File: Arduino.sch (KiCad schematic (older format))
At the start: 0 parts

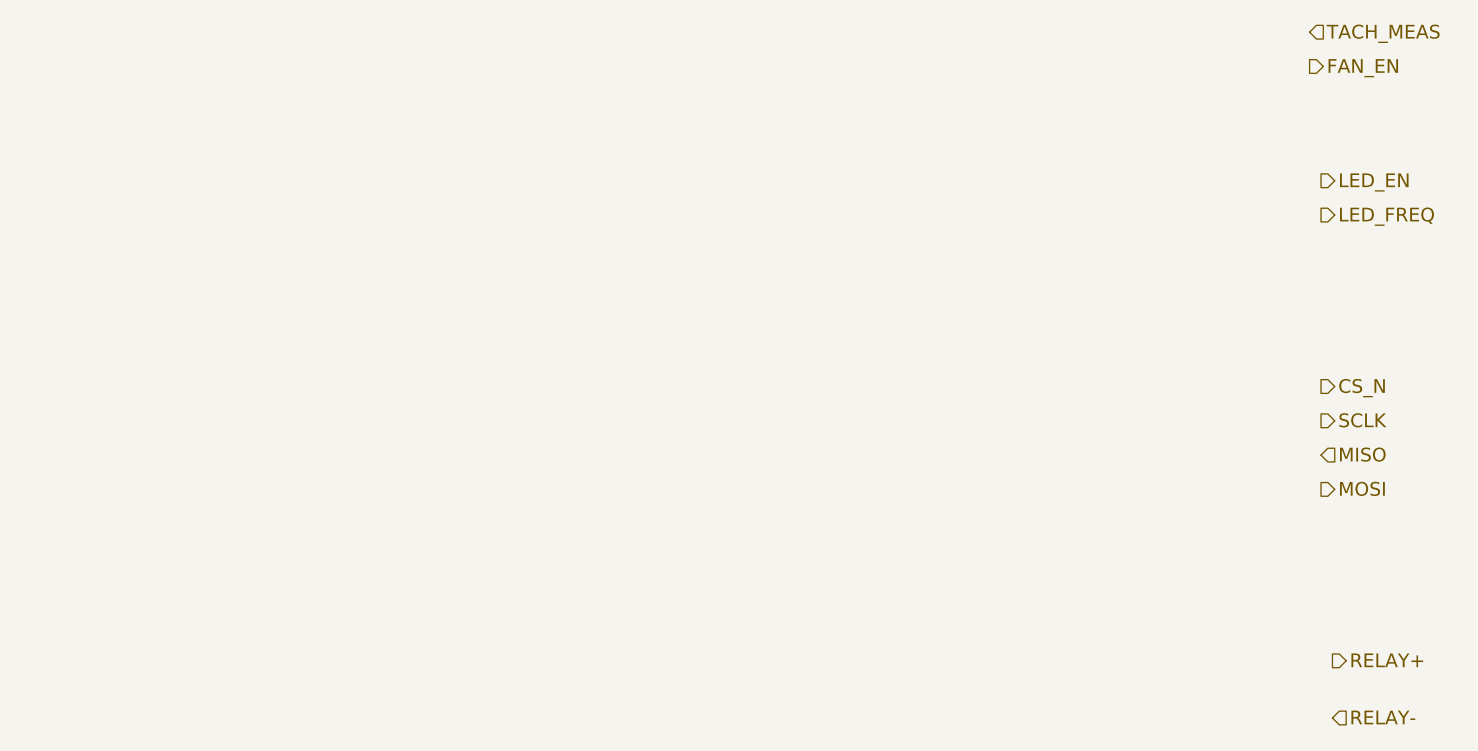
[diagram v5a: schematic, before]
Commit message: Created the Arduino module and then connected all the modules in the main schematic
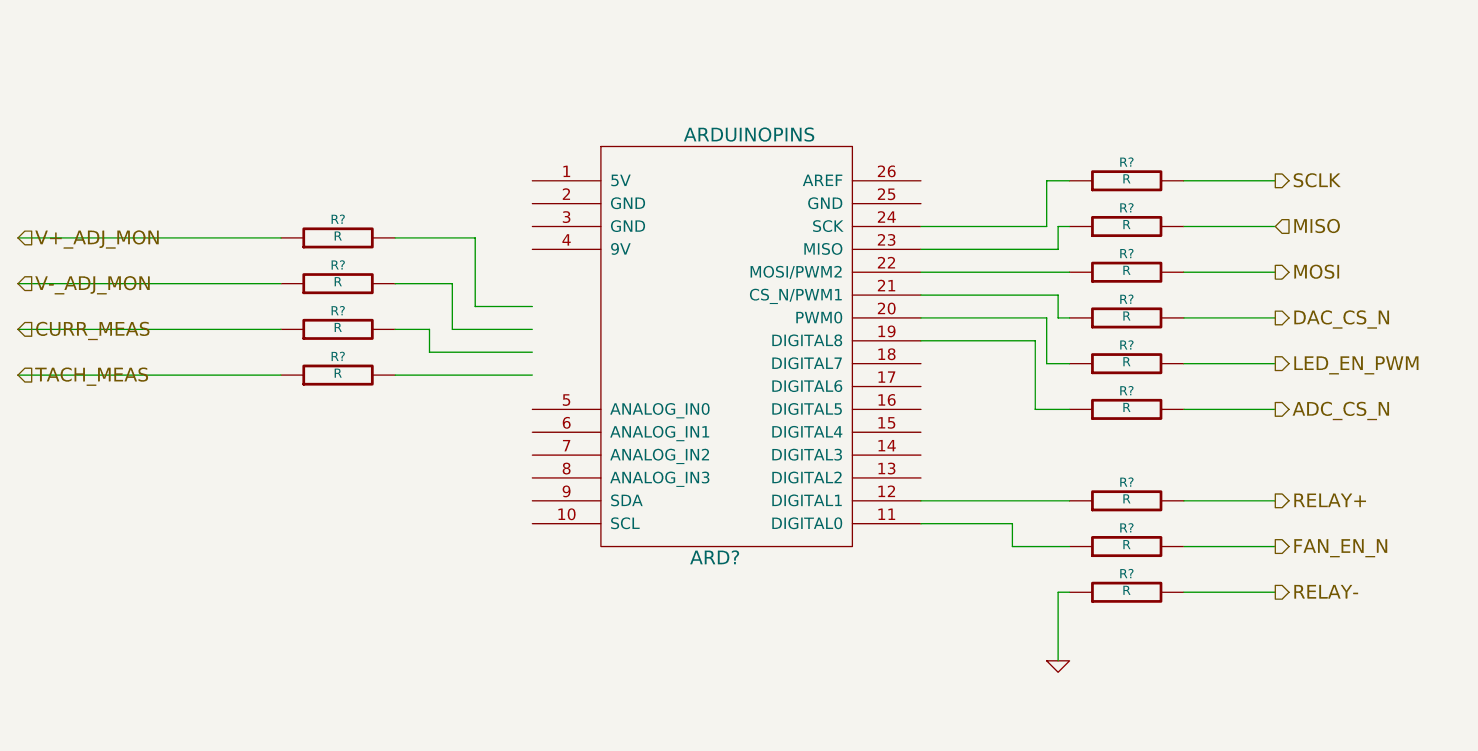
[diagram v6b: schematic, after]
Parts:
- added ARD?: ARDUINOPINS, symbol ARDUINOPINS
- added R? (x13): R, ~, symbol R
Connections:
- net labels added: ADC_CS_N, CURR_MEAS, DAC_CS_N, FAN_EN_N, GND, LED_EN_PWM, V+_ADJ_MON, V-_ADJ_MON
- net labels removed: CS_N, FAN_EN, LED_EN, LED_FREQ
- wire segments 0 -> 45

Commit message: Modified the FAN module and corresponding pins in Arduino module
1) Added FAN_MODE
2) Changed FAN_EN_N to FAN_PWM
3) Used one of the digital PWM pins for FAN_PWM
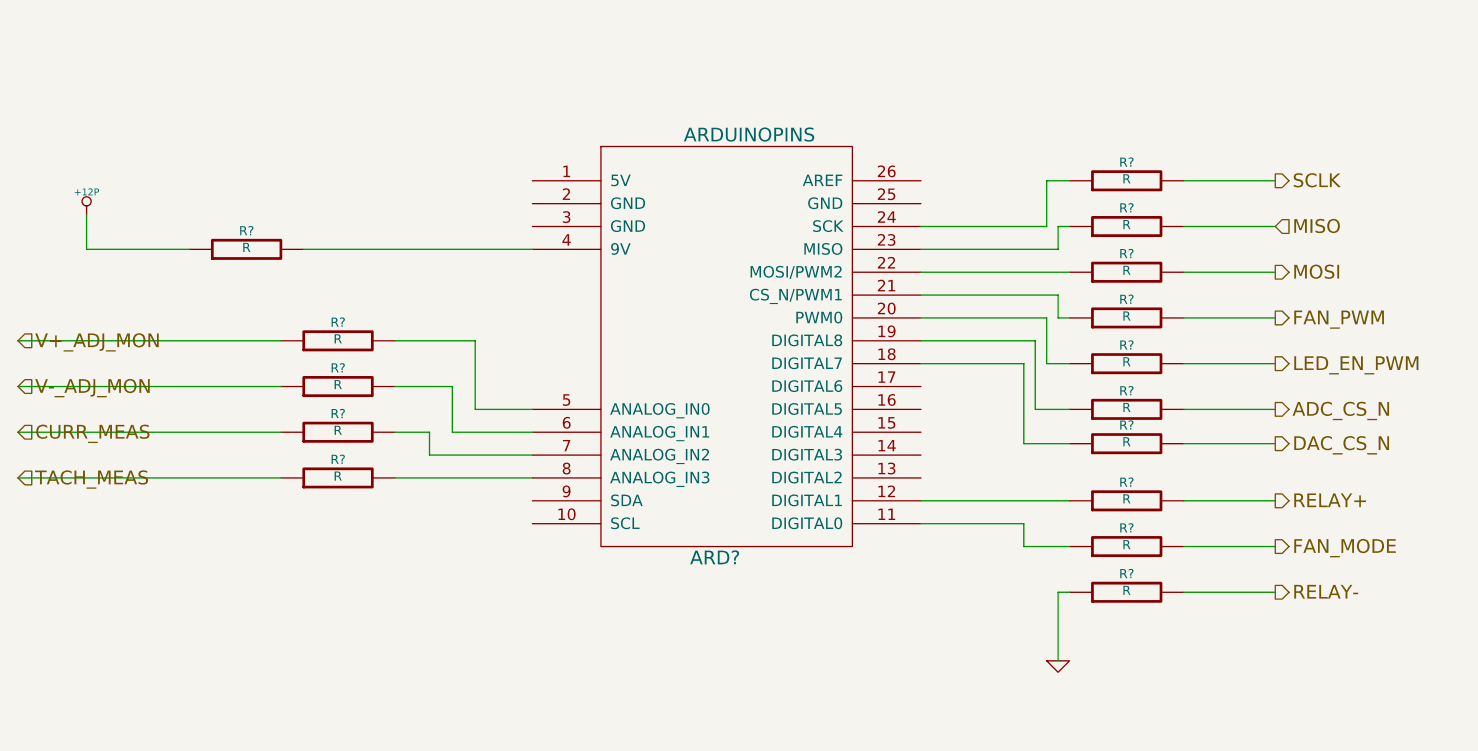
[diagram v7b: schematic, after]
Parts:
- removed ARD?: ARDUINOPINS, symbol ARDUINOPINS
- added ARD?: ARDUINOPINS, ~, symbol ARDUINOPINS
- added R? (x2): R, ~, symbol R
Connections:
- net labels added: +12P, FAN_MODE, FAN_PWM
- net labels removed: FAN_EN_N
- wire segments 45 -> 52
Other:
- moved on the sheet: R?
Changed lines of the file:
@@
 Sheet 2 9
 Title ""
-Date "10 feb 2014"
+Date "11 feb 2014"
 Rev ""
 Comp ""
@@
 Text HLabel 7000 1950 2    60   Output ~ 0
 SCLK
-Text HLabel 7000 2550 2    60   Output ~ 0
+Text HLabel 7000 3100 2    60   Output ~ 0
 DAC_CS_N
 Text HLabel 7000 2750 2    60   Output ~ 0
 LED_EN_PWM
-Text HLabel 7000 3550 2    60   Output ~ 0
-FAN_EN_N
-Text HLabel 1500 2800 2    60   Input ~ 0
+Text HLabel 7000 2550 2    60   Output ~ 0
+FAN_PWM
+Text HLabel 1500 3250 2    60   Input ~ 0
 TACH_MEAS
-$Comp
-L ARDUINOPINS ARD?
-U 1 1 52F895B2
-P 4700 3350
-F 0 "ARD?" H 4550 3100 60  0000 C CNN
-F 1 "ARDUINOPINS" H 4700 4950 60  0000 C CNN
-F 2 "" H 4700 3350 60  0000 C CNN
-F 3 "" H 4700 3350 60  0000 C CNN
-	1    4700 3350
-	1    0    0    -1
-$EndComp
-Text HLabel 1500 2600 2    60   Input ~ 0
+Text HLabel 1500 3050 2    60   Input ~ 0
 CURR_MEAS
 $Comp
 L R R?
 U 1 1 52F8B0F4
-P 6350 3550
-F 0 "R?" V 6430 3550 40  0000 C CNN
-F 1 "R" V 6357 3551 40  0000 C CNN
-F 2 "~" V 6280 3550 30  0000 C CNN
-F 3 "~" H 6350 3550 30  0000 C CNN
-	1    6350 3550
+P 6350 2550
+F 0 "R?" V 6430 2550 40  0000 C CNN
+F 1 "R" V 6357 2551 40  0000 C CNN
+F 2 "~" V 6280 2550 30  0000 C CNN
+F 3 "~" H 6350 2550 30  0000 C CNN
+	1    6350 2550
 	0    -1   -1   0
 $EndComp
@@
 L R R?
 U 1 1 52F8B730
-P 2900 2800
-F 0 "R?" V 2980 2800 40  0000 C CNN
-F 1 "R" V 2907 2801 40  0000 C CNN
-F 2 "~" V 2830 2800 30  0000 C CNN
-F 3 "~" H 2900 2800 30  0000 C CNN
-	1    2900 2800
+P 2900 3250
+F 0 "R?" V 2980 3250 40  0000 C CNN
+F 1 "R" V 2907 3251 40  0000 C CNN
+F 2 "~" V 2830 3250 30  0000 C CNN
+F 3 "~" H 2900 3250 30  0000 C CNN
+	1    2900 3250
 	0    -1   -1   0
 $EndComp
@@
 L R R?
 U 1 1 52F8B760
-P 2900 2600
-F 0 "R?" V 2980 2600 40  0000 C CNN
-F 1 "R" V 2907 2601 40  0000 C CNN
-F 2 "~" V 2830 2600 30  0000 C CNN
-F 3 "~" H 2900 2600 30  0000 C CNN
-	1    2900 2600
-	0    -1   -1   0
-$EndComp
-Text HLabel 1500 2200 2    60   Input ~ 0
+P 2900 3050
+F 0 "R?" V 2980 3050 40  0000 C CNN
+F 1 "R" V 2907 3051 40  0000 C CNN
+F 2 "~" V 2830 3050 30  0000 C CNN
+F 3 "~" H 2900 3050 30  0000 C CNN
+	1    2900 3050
+	0    -1   -1   0
+$EndComp
+Text HLabel 1500 2650 2    60   Input ~ 0
 V+_ADJ_MON
-Text HLabel 1500 2400 2    60   Input ~ 0
+Text HLabel 1500 2850 2    60   Input ~ 0
 V-_ADJ_MON
 $Comp
 L R R?
 U 1 1 52F8BEB6
-P 2900 2400
-F 0 "R?" V 2980 2400 40  0000 C CNN
-F 1 "R" V 2907 2401 40  0000 C CNN
-F 2 "~" V 2830 2400 30  0000 C CNN
-F 3 "~" H 2900 2400 30  0000 C CNN
-	1    2900 2400
+P 2900 2850
+F 0 "R?" V 2980 2850 40  0000 C CNN
+F 1 "R" V 2907 2851 40  0000 C CNN
+F 2 "~" V 2830 2850 30  0000 C CNN
+F 3 "~" H 2900 2850 30  0000 C CNN
+	1    2900 2850
 	0    -1   -1   0
 $EndComp
@@
 L R R?
 U 1 1 52F8BEBC
-P 2900 2200
-F 0 "R?" V 2980 2200 40  0000 C CNN
-F 1 "R" V 2907 2201 40  0000 C CNN
-F 2 "~" V 2830 2200 30  0000 C CNN
-F 3 "~" H 2900 2200 30  0000 C CNN
-	1    2900 2200
+P 2900 2650
+F 0 "R?" V 2980 2650 40  0000 C CNN
+F 1 "R" V 2907 2651 40  0000 C CNN
+F 2 "~" V 2830 2650 30  0000 C CNN
+F 3 "~" H 2900 2650 30  0000 C CNN
+	1    2900 2650
 	0    -1   -1   0
 $EndComp
@@
 L R R?
 U 1 1 52F8BF34
-P 6350 2550
-F 0 "R?" V 6430 2550 40  0000 C CNN
-F 1 "R" V 6357 2551 40  0000 C CNN
-F 2 "~" V 6280 2550 30  0000 C CNN
-F 3 "~" H 6350 2550 30  0000 C CNN
-	1    6350 2550
+P 6350 3100
+F 0 "R?" V 6430 3100 40  0000 C CNN
+F 1 "R" V 6357 3101 40  0000 C CNN
+F 2 "~" V 6280 3100 30  0000 C CNN
+F 3 "~" H 6350 3100 30  0000 C CNN
+	1    6350 3100
 	0    -1   -1   0
 $EndComp
@@
 $EndComp
 Wire Wire Line
-	5450 3450 5850 3450
-Wire Wire Line
-	5850 3450 5850 3550
-Wire Wire Line
-	5850 3550 6100 3550
+	5450 2450 6050 2450
 Wire Wire Line
 	5450 3350 6100 3350
@@
 	6600 3350 7000 3350
 Wire Wire Line
-	6600 3550 7000 3550
+	6600 2550 7000 2550
 Wire Wire Line
 	6600 3750 7000 3750
@@
 	6050 3750 6050 4050
 Wire Wire Line
-	3750 2800 3150 2800
-Wire Wire Line
-	1500 2800 2650 2800
-Wire Wire Line
-	3750 2700 3300 2700
-Wire Wire Line
-	3300 2700 3300 2600
-Wire Wire Line
-	3300 2600 3150 2600
-Wire Wire Line
-	1500 2600 2650 2600
-Wire Wire Line
-	3750 2600 3400 2600
-Wire Wire Line
-	3400 2600 3400 2400
-Wire Wire Line
-	3400 2400 3150 2400
-Wire Wire Line
-	3750 2500 3500 2500
-Wire Wire Line
-	3500 2500 3500 2200
-Wire Wire Line
-	3500 2200 3150 2200
-Wire Wire Line
-	2650 2400 1500 2400
-Wire Wire Line
-	1500 2200 2650 2200
-Wire Wire Line
-	7000 2550 6600 2550
+	3750 3250 3150 3250
+Wire Wire Line
+	1500 3250 2650 3250
+Wire Wire Line
+	3750 3150 3300 3150
+Wire Wire Line
+	3300 3150 3300 3050
+Wire Wire Line
+	3300 3050 3150 3050
+Wire Wire Line
+	1500 3050 2650 3050
+Wire Wire Line
+	3750 3050 3400 3050
+Wire Wire Line
+	3400 3050 3400 2850
+Wire Wire Line
+	3400 2850 3150 2850
+Wire Wire Line
+	3750 2950 3500 2950
+Wire Wire Line
+	3500 2950 3500 2650
+Wire Wire Line
+	3500 2650 3150 2650
+Wire Wire Line
+	2650 2850 1500 2850
+Wire Wire Line
+	1500 2650 2650 2650
+Wire Wire Line
+	7000 3100 6600 3100
 Wire Wire Line
 	7000 2350 6600 2350
@@
 	7000 1950 6600 1950
 Wire Wire Line
-	5450 2450 6050 2450
-Wire Wire Line
-	6050 2450 6050 2550
-Wire Wire Line
-	6050 2550 6100 2550
+	5900 3100 6100 3100
 Wire Wire Line
 	5450 2350 6100 2350
@@
 Wire Wire Line
 	5950 2950 6100 2950
+Wire Wire Line
+	5900 3100 5900 2750
+Wire Wire Line
+	5900 2750 5450 2750
+Wire Wire Line
+	6050 2550 6100 2550
+Wire Wire Line
+	6050 2450 6050 2550
+Text HLabel 7000 3550 2    60   Output ~ 0
+FAN_MODE
+$Comp
+L R R?
+U 1 1 52F9FE44
+P 6350 3550
+F 0 "R?" V 6430 3550 40  0000 C CNN
+F 1 "R" V 6357 3551 40  0000 C CNN
+F 2 "~" V 6280 3550 30  0000 C CNN
+F 3 "~" H 6350 3550 30  0000 C CNN
+	1    6350 3550
+	0    -1   -1   0
+$EndComp
+Wire Wire Line
+	5900 3550 6100 3550
+Wire Wire Line
+	5450 3450 5900 3450
+Wire Wire Line
+	5900 3450 5900 3550
+Wire Wire Line
+	7000 3550 6600 3550
+$Comp
+L ARDUINOPINS ARD?
+U 1 1 52F9FF33
+P 4700 3350
+F 0 "ARD?" H 4550 3100 60  0000 C CNN
+F 1 "ARDUINOPINS" H 4700 4950 60  0000 C CNN
+F 2 "~" H 4700 3350 60  0000 C CNN
+F 3 "~" H 4700 3350 60  0000 C CNN
+	1    4700 3350
+	1    0    0    -1
+$EndComp
+$Comp
+L R R?
+U 1 1 52F9FF40
+P 2500 2250
+F 0 "R?" V 2580 2250 40  0000 C CNN
+F 1 "R" V 2507 2251 40  0000 C CNN
+F 2 "~" V 2430 2250 30  0000 C CNN
+F 3 "~" H 2500 2250 30  0000 C CNN
+	1    2500 2250
+	0    -1   -1   0
+$EndComp
+Wire Wire Line
+	3750 2250 2750 2250
+Wire Wire Line
+	2250 2250 1800 2250
+Wire Wire Line
+	1800 2250 1800 2100
+$Comp
+L +12P #PWR?
+U 1 1 52F9FFAF
+P 1800 2100
+F 0 "#PWR?" H 1800 2070 30  0001 C CNN
+F 1 "+12P" H 1800 2200 30  0000 C CNN
+F 2 "" H 1800 2100 60  0000 C CNN
+F 3 "" H 1800 2100 60  0000 C CNN
+	1    1800 2100
+	1    0    0    -1
+$EndComp
 $EndSCHEMATC

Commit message: RELAY 02-20-2014
1) Created and associated footprints for relay module
2) Placed relay module's components in PCB layout
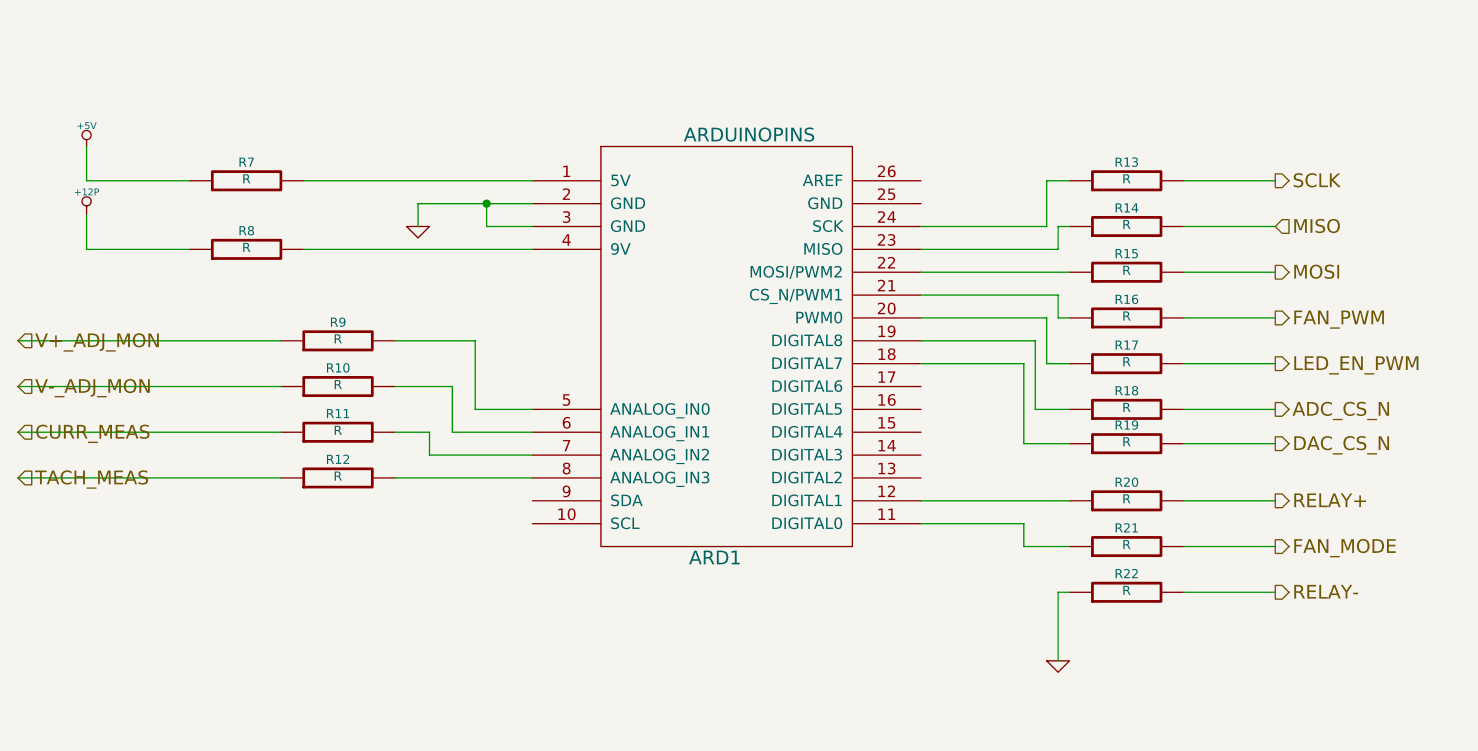
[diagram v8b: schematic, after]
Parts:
- added R7: R, ~, symbol R
- gave numbers to parts that had none: 16
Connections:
- net GND: now also ARD1.2 (GND), ARD1.3 (GND)
- net at ARD1.1 (5V): now also R7.2
- new net +5V: R7.1
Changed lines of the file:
@@
 Sheet 2 9
 Title ""
-Date "11 feb 2014"
+Date "20 feb 2014"
 Rev ""
 Comp ""
@@
 CURR_MEAS
 $Comp
-L R R?
+L R R16
 U 1 1 52F8B0F4
 P 6350 2550
-F 0 "R?" V 6430 2550 40  0000 C CNN
+F 0 "R16" V 6430 2550 40  0000 C CNN
 F 1 "R" V 6357 2551 40  0000 C CNN
 F 2 "~" V 6280 2550 30  0000 C CNN
@@
 $EndComp
 $Comp
-L R R?
+L R R20
 U 1 1 52F8B683
 P 6350 3350
-F 0 "R?" V 6430 3350 40  0000 C CNN
+F 0 "R20" V 6430 3350 40  0000 C CNN
 F 1 "R" V 6357 3351 40  0000 C CNN
 F 2 "~" V 6280 3350 30  0000 C CNN
@@
 $EndComp
 $Comp
-L GND #PWR?
+L GND #PWR4
 U 1 1 52F8B714
 P 6050 4050
-F 0 "#PWR?" H 6050 4050 30  0001 C CNN
+F 0 "#PWR4" H 6050 4050 30  0001 C CNN
 F 1 "GND" H 6050 3980 30  0001 C CNN
 F 2 "" H 6050 4050 60  0000 C CNN
@@
 $EndComp
 $Comp
-L R R?
+L R R12
 U 1 1 52F8B730
 P 2900 3250
-F 0 "R?" V 2980 3250 40  0000 C CNN
+F 0 "R12" V 2980 3250 40  0000 C CNN
 F 1 "R" V 2907 3251 40  0000 C CNN
 F 2 "~" V 2830 3250 30  0000 C CNN
@@
 $EndComp
 $Comp
-L R R?
+L R R11
 U 1 1 52F8B760
 P 2900 3050
-F 0 "R?" V 2980 3050 40  0000 C CNN
+F 0 "R11" V 2980 3050 40  0000 C CNN
 F 1 "R" V 2907 3051 40  0000 C CNN
 F 2 "~" V 2830 3050 30  0000 C CNN
@@
 V-_ADJ_MON
 $Comp
-L R R?
+L R R10
 U 1 1 52F8BEB6
 P 2900 2850
-F 0 "R?" V 2980 2850 40  0000 C CNN
+F 0 "R10" V 2980 2850 40  0000 C CNN
 F 1 "R" V 2907 2851 40  0000 C CNN
 F 2 "~" V 2830 2850 30  0000 C CNN
@@
 $EndComp
 $Comp
-L R R?
+L R R9
 U 1 1 52F8BEBC
 P 2900 2650
-F 0 "R?" V 2980 2650 40  0000 C CNN
+F 0 "R9" V 2980 2650 40  0000 C CNN
 F 1 "R" V 2907 2651 40  0000 C CNN
 F 2 "~" V 2830 2650 30  0000 C CNN
@@
 $EndComp
 $Comp
-L R R?
+L R R19
 U 1 1 52F8BF34
 P 6350 3100
-F 0 "R?" V 6430 3100 40  0000 C CNN
+F 0 "R19" V 6430 3100 40  0000 C CNN
 F 1 "R" V 6357 3101 40  0000 C CNN
 F 2 "~" V 6280 3100 30  0000 C CNN
@@
 $EndComp
 $Comp
-L R R?
+L R R15
 U 1 1 52F8BF4E
 P 6350 2350
-F 0 "R?" V 6430 2350 40  0000 C CNN
+F 0 "R15" V 6430 2350 40  0000 C CNN
 F 1 "R" V 6357 2351 40  0000 C CNN
 F 2 "~" V 6280 2350 30  0000 C CNN
@@
 $EndComp
 $Comp
-L R R?
+L R R14
 U 1 1 52F8BF54
 P 6350 2150
-F 0 "R?" V 6430 2150 40  0000 C CNN
+F 0 "R14" V 6430 2150 40  0000 C CNN
 F 1 "R" V 6357 2151 40  0000 C CNN
 F 2 "~" V 6280 2150 30  0000 C CNN
@@
 $EndComp
 $Comp
-L R R?
+L R R13
 U 1 1 52F8BF5A
 P 6350 1950
-F 0 "R?" V 6430 1950 40  0000 C CNN
+F 0 "R13" V 6430 1950 40  0000 C CNN
 F 1 "R" V 6357 1951 40  0000 C CNN
 F 2 "~" V 6280 1950 30  0000 C CNN
@@
 	6000 1950 6100 1950
 $Comp
-L R R?
+L R R22
 U 1 1 52F8C0B1
 P 6350 3750
-F 0 "R?" V 6430 3750 40  0000 C CNN
+F 0 "R22" V 6430 3750 40  0000 C CNN
 F 1 "R" V 6357 3751 40  0000 C CNN
 F 2 "~" V 6280 3750 30  0000 C CNN
@@
 	6100 3750 6050 3750
 $Comp
-L R R?
+L R R17
 U 1 1 52F8C429
 P 6350 2750
-F 0 "R?" V 6430 2750 40  0000 C CNN
+F 0 "R17" V 6430 2750 40  0000 C CNN
 F 1 "R" V 6357 2751 40  0000 C CNN
 F 2 "~" V 6280 2750 30  0000 C CNN
@@
 ADC_CS_N
 $Comp
-L R R?
+L R R18
 U 1 1 52F912F6
 P 6350 2950
-F 0 "R?" V 6430 2950 40  0000 C CNN
+F 0 "R18" V 6430 2950 40  0000 C CNN
 F 1 "R" V 6357 2951 40  0000 C CNN
 F 2 "~" V 6280 2950 30  0000 C CNN
@@
 FAN_MODE
 $Comp
-L R R?
+L R R21
 U 1 1 52F9FE44
 P 6350 3550
-F 0 "R?" V 6430 3550 40  0000 C CNN
+F 0 "R21" V 6430 3550 40  0000 C CNN
 F 1 "R" V 6357 3551 40  0000 C CNN
 F 2 "~" V 6280 3550 30  0000 C CNN
@@
 	7000 3550 6600 3550
 $Comp
-L ARDUINOPINS ARD?
+L ARDUINOPINS ARD1
 U 1 1 52F9FF33
 P 4700 3350
-F 0 "ARD?" H 4550 3100 60  0000 C CNN
+F 0 "ARD1" H 4550 3100 60  0000 C CNN
 F 1 "ARDUINOPINS" H 4700 4950 60  0000 C CNN
 F 2 "~" H 4700 3350 60  0000 C CNN
@@
 $EndComp
 $Comp
-L R R?
+L R R8
 U 1 1 52F9FF40
 P 2500 2250
-F 0 "R?" V 2580 2250 40  0000 C CNN
+F 0 "R8" V 2580 2250 40  0000 C CNN
 F 1 "R" V 2507 2251 40  0000 C CNN
 F 2 "~" V 2430 2250 30  0000 C CNN
@@
 	1800 2250 1800 2100
 $Comp
-L +12P #PWR?
+L +12P #PWR2
 U 1 1 52F9FFAF
 P 1800 2100
-F 0 "#PWR?" H 1800 2070 30  0001 C CNN
+F 0 "#PWR2" H 1800 2070 30  0001 C CNN
 F 1 "+12P" H 1800 2200 30  0000 C CNN
 F 2 "" H 1800 2100 60  0000 C CNN
@@
 	1    0    0    -1
 $EndComp
+$Comp
+L R R7
+U 1 1 5302EB0F
+P 2500 1950
+F 0 "R7" V 2580 1950 40  0000 C CNN
+F 1 "R" V 2507 1951 40  0000 C CNN
+F 2 "~" V 2430 1950 30  0000 C CNN
+F 3 "~" H 2500 1950 30  0000 C CNN
+	1    2500 1950
+	0    -1   -1   0
+$EndComp
+Wire Wire Line
+	3750 1950 2750 1950
+Wire Wire Line
+	2250 1950 1800 1950
+Wire Wire Line
+	1800 1950 1800 1800
+$Comp
+L +5V #PWR1
+U 1 1 5302EB20
+P 1800 1800
+F 0 "#PWR1" H 1800 1890 20  0001 C CNN
+F 1 "+5V" H 1800 1890 30  0000 C CNN
+F 2 "" H 1800 1800 60  0000 C CNN
+F 3 "" H 1800 1800 60  0000 C CNN
+	1    1800 1800
+	1    0    0    -1
+$EndComp
+Wire Wire Line
+	3750 2050 3250 2050
+Wire Wire Line
+	3750 2150 3550 2150
+Wire Wire Line
+	3550 2150 3550 2050
+Connection ~ 3550 2050
+$Comp
+L GND #PWR3
+U 1 1 5302EB9F
+P 3250 2150
+F 0 "#PWR3" H 3250 2150 30  0001 C CNN
+F 1 "GND" H 3250 2080 30  0001 C CNN
+F 2 "" H 3250 2150 60  0000 C CNN
+F 3 "" H 3250 2150 60  0000 C CNN
+	1    3250 2150
+	1    0    0    -1
+$EndComp
+Wire Wire Line
+	3250 2050 3250 2150
 $EndSCHEMATC
